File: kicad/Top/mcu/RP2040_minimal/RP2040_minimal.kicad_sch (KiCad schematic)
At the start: 34 parts, among them J1 USB_B_Micro, J2 Conn_01x02, J3 Conn_02x18_Odd_Even, J4 Conn_02x18_Odd_Even, U1 NCP1117-3.3_SOT223, U2 W25Q128JVS, U3 RP2040, Y1 ABLS-12.000MHZ-B4-T

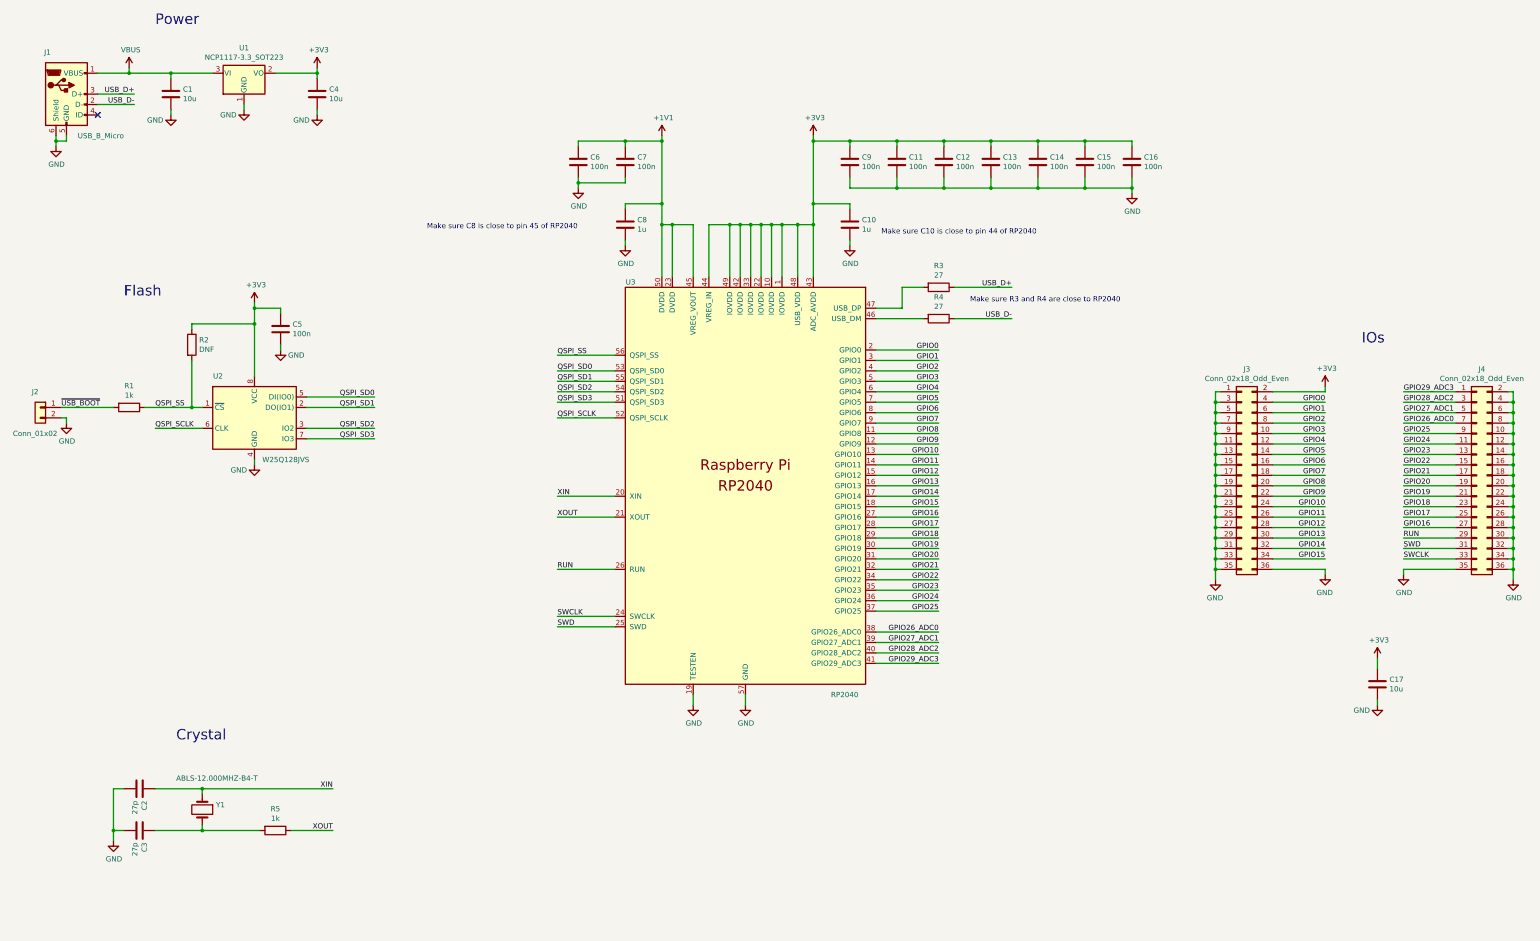
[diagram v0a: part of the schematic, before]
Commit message: Added hierarchial pins to mcu
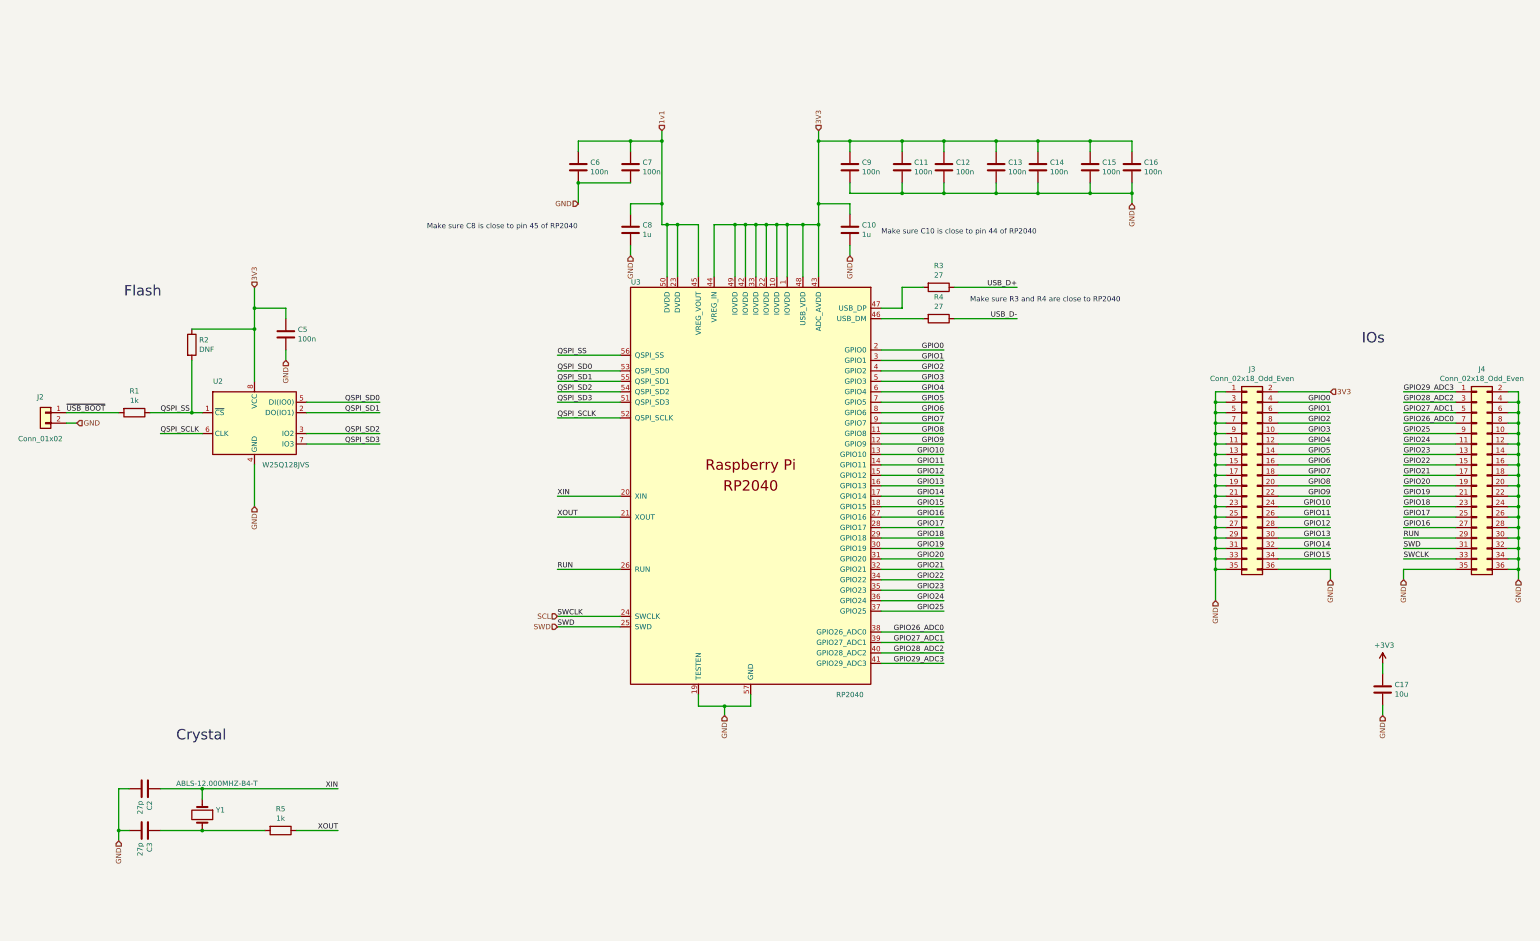
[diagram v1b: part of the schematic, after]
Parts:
- removed C1, C4: 10u, Capacitor_SMD:C_0805_2012Metric, symbol Device:C
- removed J1: USB_B_Micro, RP2040_minimal:USB_Micro-B_Amphenol_10103594-0001LF_Horizontal_modified, symbol RP2040_minimal-rescue:USB_B_Micro-Connector
- removed U1: NCP1117-3.3_SOT223, Package_TO_SOT_SMD:SOT-223-3_TabPin2, symbol Regulator_Linear:NCP1117-3.3_SOT223
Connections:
- net +3V3: no longer C10.1, C11.1, C12.1, C13.1, C14.1, C15.1, C16.1, C5.1, C9.1, J3.2 (Pin_2), R2.1, U2.8 (VCC), U3.1 (IOVDD), U3.10 (IOVDD), U3.22 (IOVDD), U3.33 (IOVDD), U3.42 (IOVDD), U3.43 (ADC_AVDD), U3.44 (VREG_IN), U3.48 (USB_VDD), U3.49 (IOVDD)
- net +1V1 renamed 1v1
- net SWCLK renamed SCL
- new net 3V3: C10.1, C11.1, C12.1, C13.1, C14.1, C15.1, C16.1, C5.1, C9.1, J3.2 (Pin_2), R2.1, U2.8 (VCC), U3.1 (IOVDD), U3.10 (IOVDD), U3.22 (IOVDD), U3.33 (IOVDD), U3.42 (IOVDD), U3.43 (ADC_AVDD), U3.44 (VREG_IN), U3.48 (USB_VDD), U3.49 (IOVDD)
- no-connect marks 1 -> 0
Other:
- note removed: "Power"
- moved on the sheet: C10, C11, C12, C13, C14, C15, C16, C17, C2, C3, C5, C6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

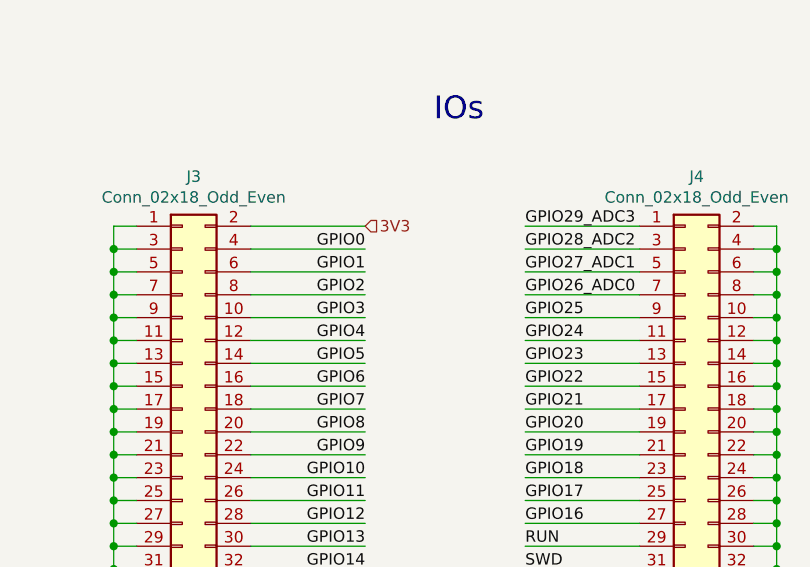
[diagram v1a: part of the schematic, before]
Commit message: Wired up MCU to PowerMux
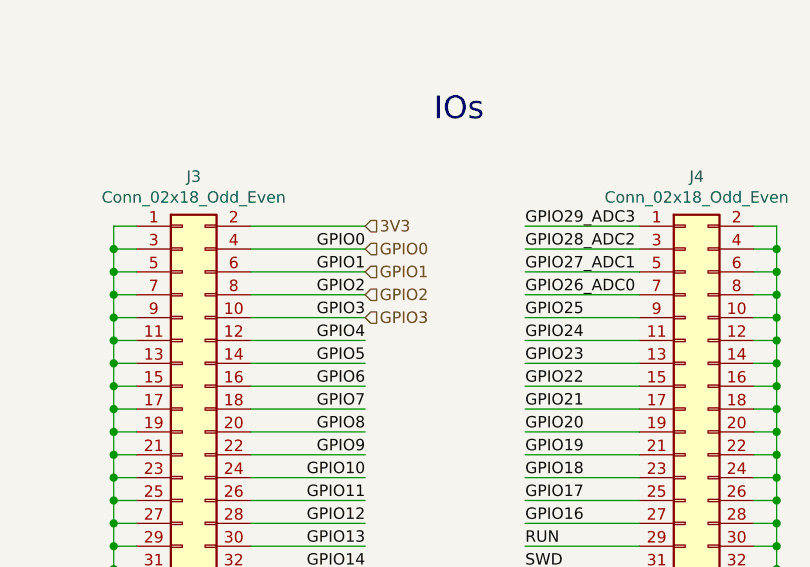
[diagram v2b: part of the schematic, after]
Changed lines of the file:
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@@
     (effects (font (size 1.27 1.27)) (justify right))
   )
+  (hierarchical_label "GPIO0" (shape input) (at 340.36 124.46 0)
+    (effects (font (size 1.27 1.27)) (justify left))
+  )
   (hierarchical_label "3V3" (shape input) (at 215.9 58.42 90)
+    (effects (font (size 1.27 1.27)) (justify left))
+  )
+  (hierarchical_label "GPIO2" (shape input) (at 340.36 129.54 0)
     (effects (font (size 1.27 1.27)) (justify left))
   )
@@
     (effects (font (size 1.27 1.27)) (justify left))
   )
+  (hierarchical_label "GPIO3" (shape input) (at 340.36 132.08 0)
+    (effects (font (size 1.27 1.27)) (justify left))
+  )
   (hierarchical_label "GND" (shape input) (at 353.06 200.66 270)
     (effects (font (size 1.27 1.27)) (justify right))
@@
     (effects (font (size 1.27 1.27)) (justify left))
   )
+  (hierarchical_label "GPIO1" (shape input) (at 340.36 127 0)
+    (effects (font (size 1.27 1.27)) (justify left))
+  )

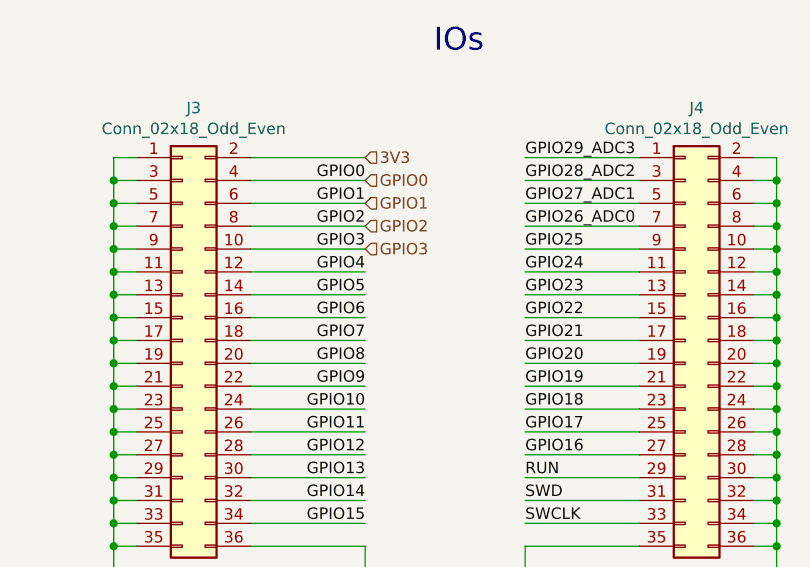
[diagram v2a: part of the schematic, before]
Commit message: Adding a few more higher level connections
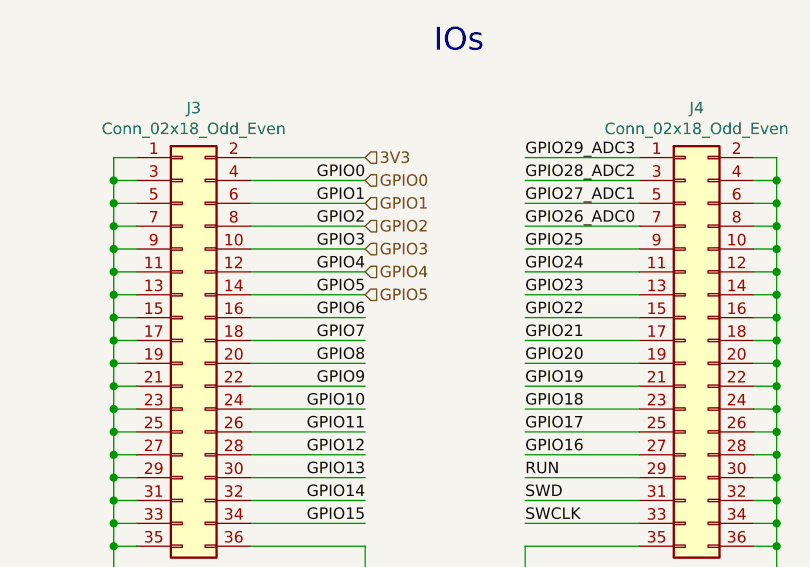
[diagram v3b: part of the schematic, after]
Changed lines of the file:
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@@
     (effects (font (size 1.27 1.27)) (justify right bottom))
+  )
+  (hierarchical_label "GPIO4" (shape input) (at 340.36 134.62 0)
+    (effects (font (size 1.27 1.27)) (justify left))
   )
   (hierarchical_label "GND" (shape input) (at 223.52 88.9 270)
@@
     (effects (font (size 1.27 1.27)) (justify right))
   )
+  (hierarchical_label "GPIO5" (shape input) (at 340.36 137.16 0)
+    (effects (font (size 1.27 1.27)) (justify left))
+  )
   (hierarchical_label "1v1" (shape input) (at 177.8 58.42 90)

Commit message: wip
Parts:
- removed J3, J4: Conn_02x18_Odd_Even, Connector_PinHeader_2.54mm:PinHeader_2x18_P2.54mm_Vertical, symbol Connector_Generic:Conn_02x18_Odd_Even
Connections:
- net 1v1: no longer names the net of C6.1, C7.1, C8.1, U3.23 (DVDD), U3.45 (VREG_VOUT), U3.50 (DVDD)
- net GPIO6 renamed I2C1_SDA
- net GPIO7 renamed I2C1_SCL
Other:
- note removed: "IOs"

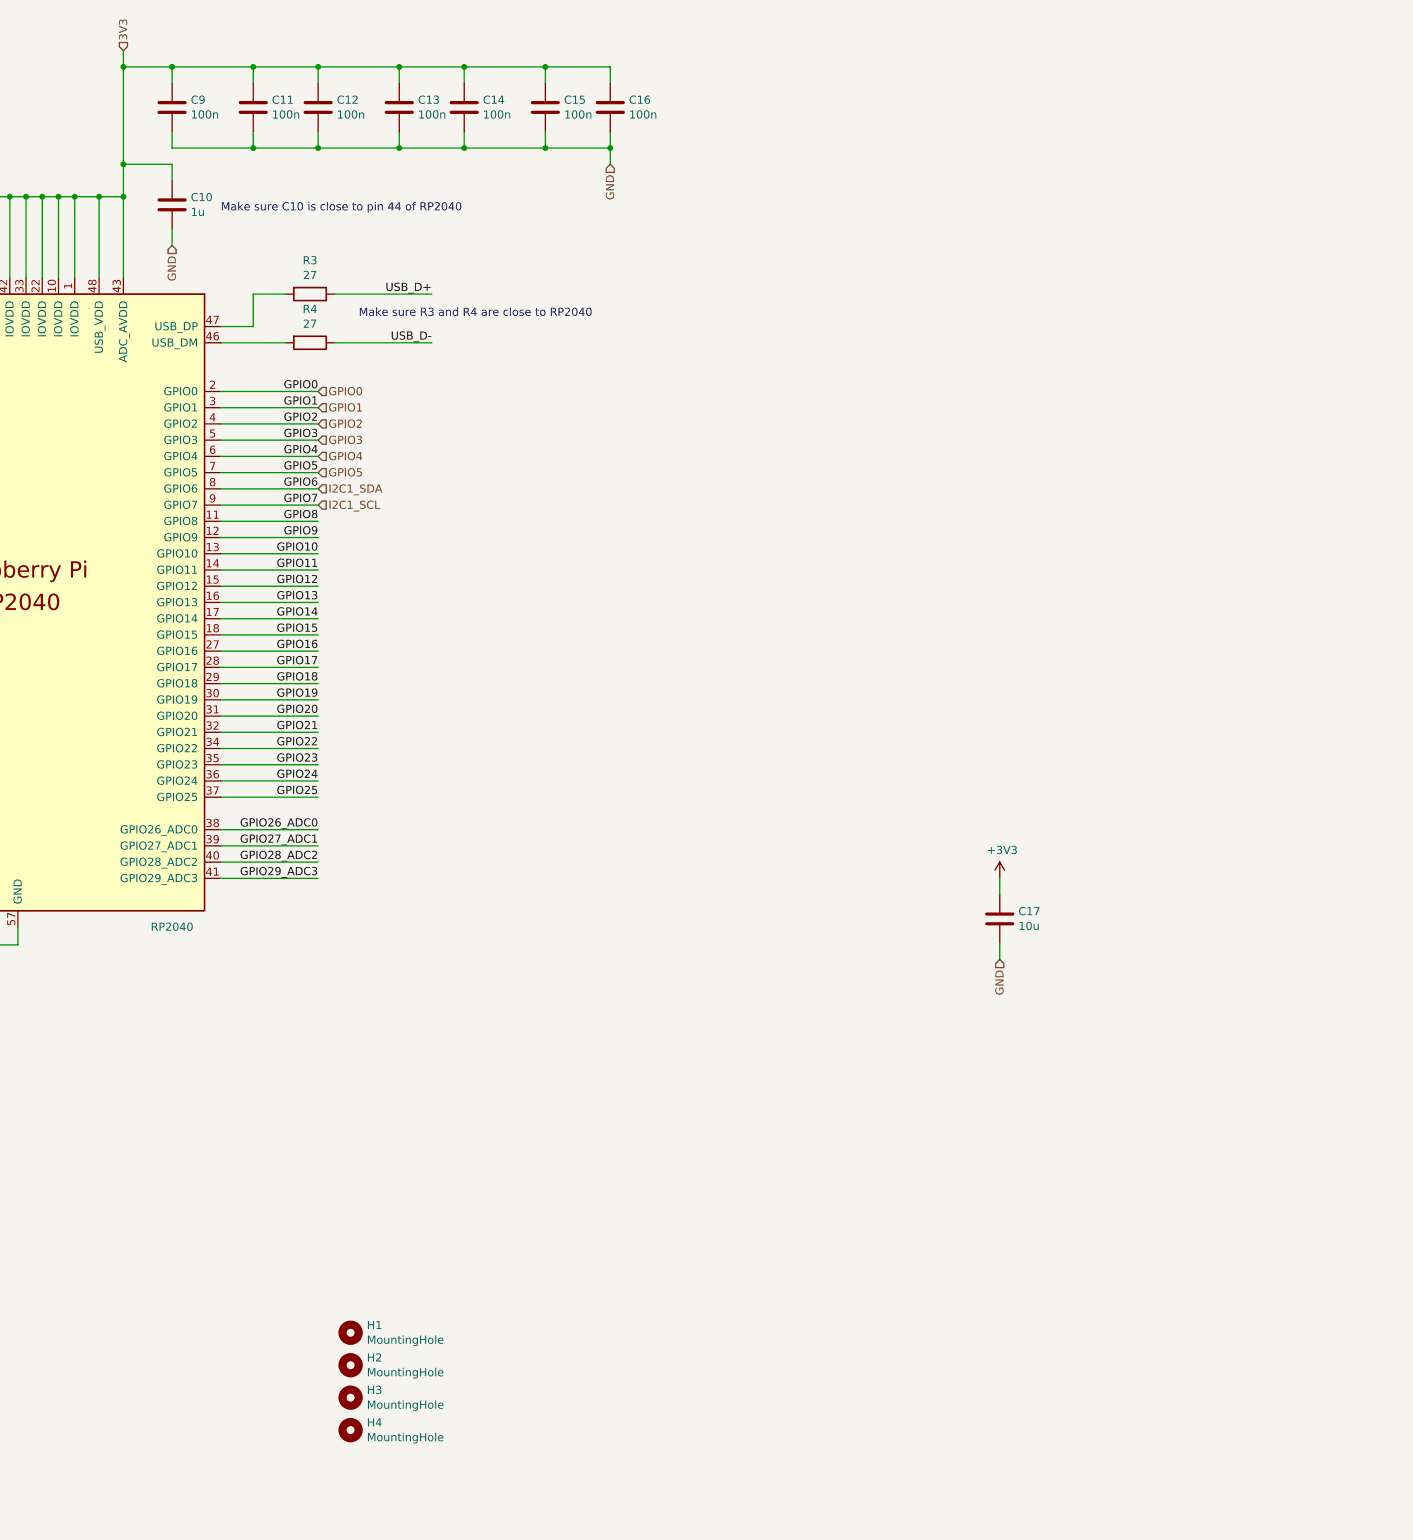
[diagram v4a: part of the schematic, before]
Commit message: Added overvoltage protection and filtering to ADC inputs of MCU
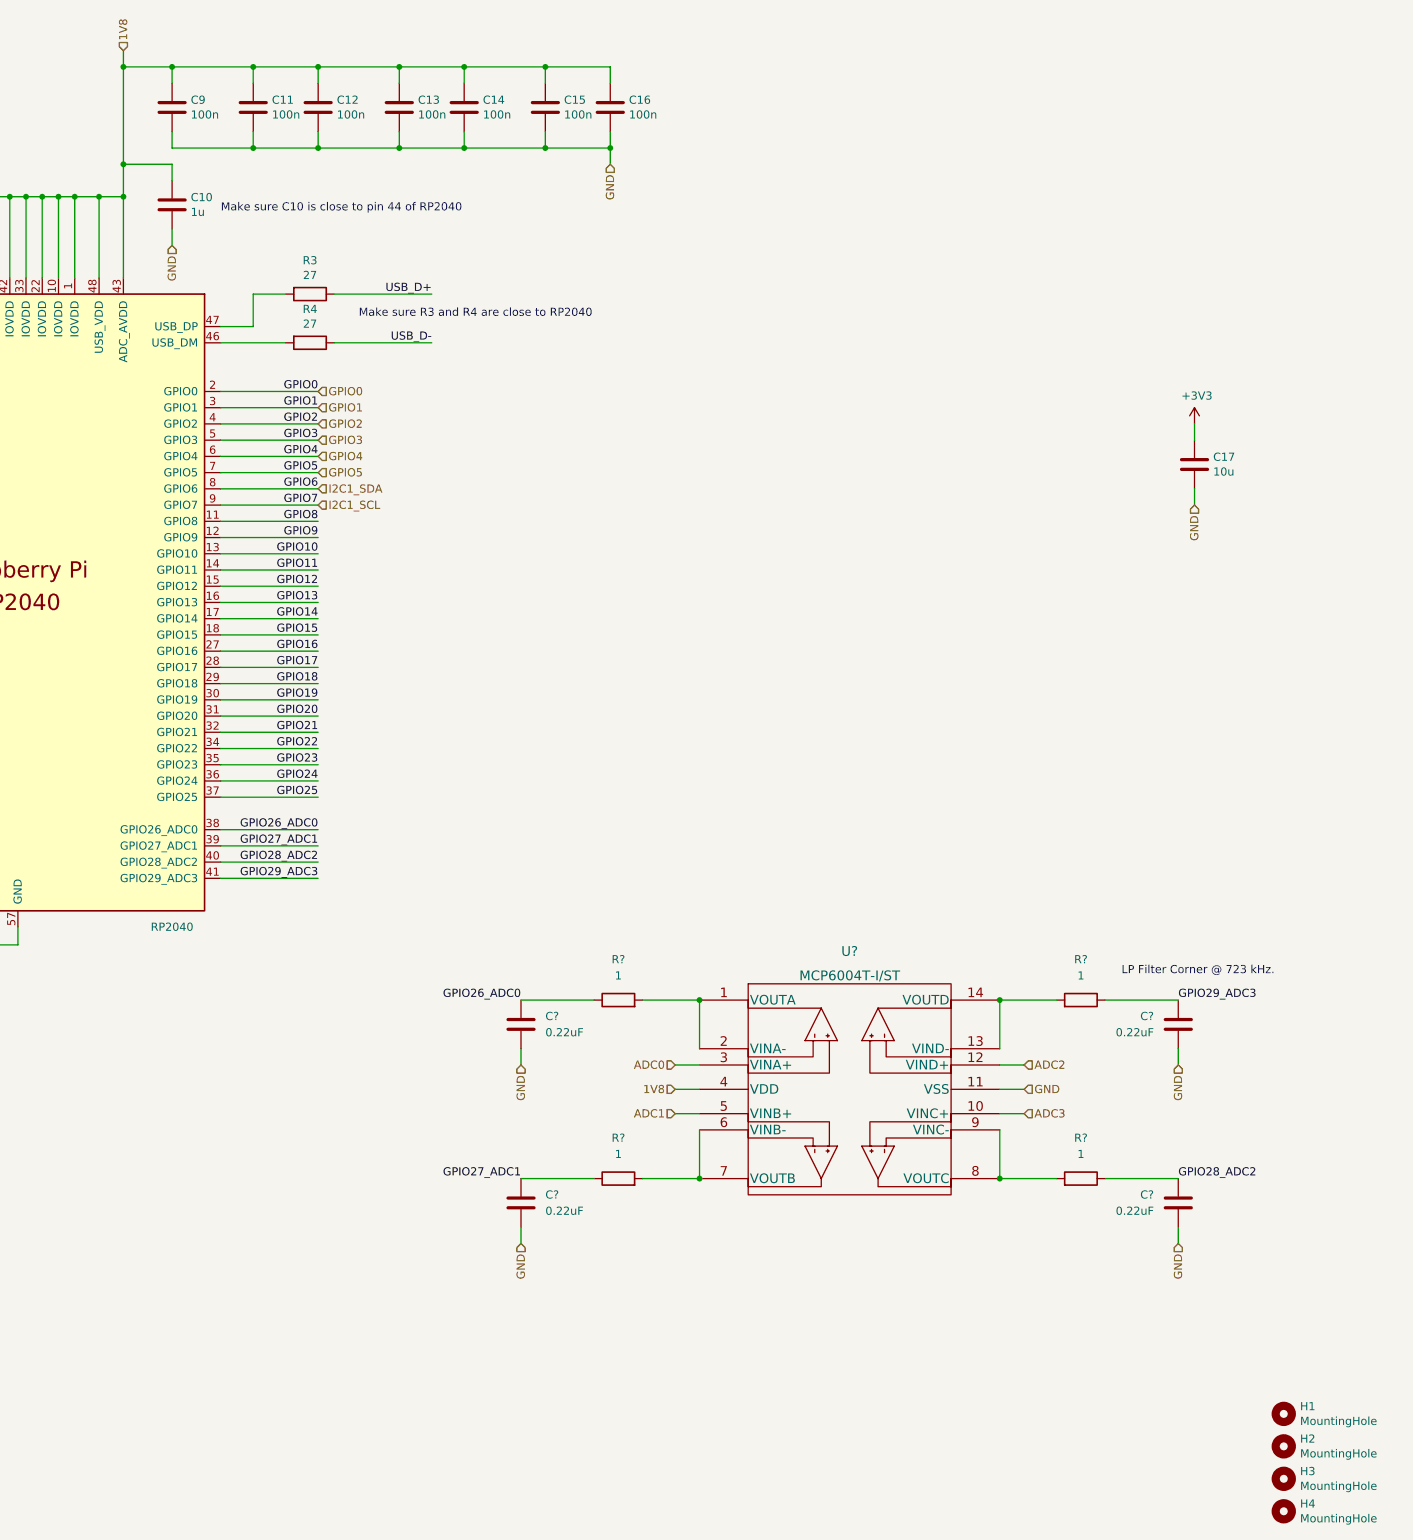
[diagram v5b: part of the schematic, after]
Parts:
- added C? (x4): 0.22uF, symbol Device:C
- added R? (x4): 1, symbol Device:R
- added U?: MCP6004T-I/ST, custom_amplifiers:MCP6004T-I&slash_ST, symbol custom_amplifiers:MCP6004T-I{brace}slash}ST
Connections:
- net 3V3: no longer C10.1, C11.1, C12.1, C13.1, C14.1, C15.1, C16.1, C9.1, U3.1 (IOVDD), U3.10 (IOVDD), U3.22 (IOVDD), U3.33 (IOVDD), U3.42 (IOVDD), U3.43 (ADC_AVDD), U3.44 (VREG_IN), U3.48 (USB_VDD), U3.49 (IOVDD)
- net GND: now also C?.2, C?.2, C?.2, C?.2, U?.11 (VSS)
- net GPIO26_ADC0: now also C?.1, R?.1
- net GPIO27_ADC1: now also C?.1, R?.1
- net GPIO28_ADC2: now also C?.1, R?.1
- net GPIO29_ADC3: now also C?.1, R?.1
- new net: R?.2, U?.1 (VOUTA), U?.2 (VINA-)
- new net: R?.2, U?.13 (VIND-), U?.14 (VOUTD)
- new net: R?.2, U?.6 (VINB-), U?.7 (VOUTB)
- new net: R?.2, U?.8 (VOUTC), U?.9 (VINC-)
- new net 1V8: C10.1, C11.1, C12.1, C13.1, C14.1, C15.1, C16.1, C9.1, U3.1 (IOVDD), U3.10 (IOVDD), U3.22 (IOVDD), U3.33 (IOVDD), U3.42 (IOVDD), U3.43 (ADC_AVDD), U3.44 (VREG_IN), U3.48 (USB_VDD), U3.49 (IOVDD), U?.4 (VDD)
- new net ADC0: U?.3 (VINA+)
- new net ADC1: U?.5 (VINB+)
- new net ADC2: U?.12 (VIND+)
- new net ADC3: U?.10 (VINC+)
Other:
- note added: "LP Filter Corner @ 723 kHz."
- moved on the sheet: C17, H1, H2, H3, H4
